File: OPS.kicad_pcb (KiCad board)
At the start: 4 copper layers, 49 x 34 mm, 92 parts, among them J1 USB, J2 PWR, J3 Banana, J4 Banana, J5 CON_PWR, J6 CON_DATA, J7 M3, P1 TC2030, Q1 SS8050, Q2 AO3400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

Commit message: started layout
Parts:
- moved C7 0.15 mm to (65.5, 64.8)
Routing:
- net SWDIO: track 0.00 -> 10.8 mm, vias 0 -> 1
- net SWCLK: track 0.00 -> 5.74 mm, vias 0 -> 1
- net Net-(J2-PadA5): track 0.00 -> 5.71 mm
- net Net-(C29-Pad2): track 0.00 -> 5.59 mm
- net Net-(J2-PadB5): track 0.00 -> 4.66 mm
- net UOUT: track 0.00 -> 3.66 mm
- net Net-(C29-Pad1): track 0.00 -> 3.59 mm
- net INT_MP_1: track 0.00 -> 3.58 mm
- net INT_MP: track 0.00 -> 3.35 mm
- net /UIN: track 0.00 -> 3.28 mm
- net Net-(D3-Pad2): track 0.00 -> 2.49 mm
- net TSENS: track 0.00 -> 2.43 mm
- net OUT: track 0.00 -> 2.32 mm
- net TREF: track 0.00 -> 2.29 mm
- net VBUS: track 0.00 -> 2.24 mm
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- added copper zone on F.Cu, net Net-(C13-Pad2)
- added copper zone on F.Cu, net Net-(C14-Pad2)
- added copper zone on F.Cu, net Net-(C15-Pad1)
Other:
- board text added: "OPS"

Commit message: routing 60%
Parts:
- C10, C15: value 100n -> 22u; footprint otter:C_0402 -> otter:C_0805
- C16, C20, C9: value 10u -> 22u
- C17, C8: footprint Capacitor_Tantalum_SMD:CP_EIA-7343-31_Kemet-D -> Capacitor_SMD:CP_Elec_6.3x5.8
- J6: footprint Connector_PinHeader_2.00mm:PinHeader_1x07_P2.00mm_Vertical -> Connector_PinHeader_2.00mm:PinHeader_1x08_P2.00mm_Vertical
- moved SW1 21.2 mm to (81.1, 52.1)
- moved J6 3.25 mm to (60.0, 52.4)
- moved J5 2.10 mm to (52.6, 74.2)
- moved C8 1.35 mm to (57.3, 77.2)
- moved C11 1.35 mm to (63.2, 82.5)
- moved R16 1.33 mm to (80.9, 67.7), turned to 0 degrees
- moved C17 1.25 mm to (74.5, 77.7)
- moved C9 0.66 mm to (61.6, 79.8)
- moved C15 0.54 mm to (68.7, 79.8)
- moved R10 0.53 mm to (63.2, 81.7)
- moved R14 0.50 mm to (63.2, 83.3)
- moved C26 0.50 mm to (70.0, 67.4)
- moved C32 0.50 mm to (69.1, 67.4)
- moved C33 0.50 mm to (68.2, 67.4)
- moved P1 0.46 mm to (76.8, 54.1), turned to 90 degrees
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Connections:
- J6 pad 4: OUT_EN_1 -> +3V3
- J6 pad 5: INT_MP_1 -> OUT_EN_1
- J6 pad 6: SCL -> INT_MP_1
- J6 pad 7: SDA -> SCL
- U3 pad 39: LED_RED -> LED_GREEN
- U3 pad 40: LED_GREEN -> LED_RED
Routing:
- net +3V3: track 1.01 -> 109.1 mm, vias 0 -> 7
- net GND: track 0.85 -> 54.6 mm, vias 1 -> 9
- net SDA: track 1.86 -> 46.0 mm, vias 0 -> 4
- net SCL: track 1.92 -> 42.4 mm, vias 0 -> 4
- net LED_RED: track 0.00 -> 39.5 mm, vias 0 -> 2
- net INT_MP: track 3.35 -> 35.4 mm, vias 0 -> 2
- net LED_GREEN: track 0.00 -> 30.5 mm, vias 0 -> 2
- net LED_ACT: track 0.00 -> 23.2 mm, vias 0 -> 2
- net VBUS: track 2.24 -> 23.2 mm, vias 0 -> 4
- net IOUT: track 2.00 -> 20.8 mm, vias 0 -> 2
- net IOUT_1: track 1.74 -> 19.1 mm, vias 0 -> 1
- net UOUT_2: track 1.64 -> 17.9 mm, vias 0 -> 1
- net TSENS_2: track 1.78 -> 17.1 mm, vias 0 -> 1
- net INT_STUSB: track 0.99 -> 15.2 mm, vias 0 -> 2
- net OUT_EN: track 0.00 -> 12.7 mm, vias 0 -> 2
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- added copper zone on B.Cu, net GND
- added copper zone on F.Cu, net GND
- added copper zone on F.Cu, net Net-(Q2-Pad2)
- added copper zone on F.Cu, net OUT
- added copper zone on F.Cu, net VBUS

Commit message: routing 99%
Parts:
- moved C8 2.00 mm to (57.3, 79.2)
- moved J5 2.00 mm to (52.6, 76.2)
- moved J2 1.85 mm to (57.0, 68.8)
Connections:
- SW1 pad 1: Net-(R5-Pad1) -> +3V3
- SW1 pad 2: +3V3 -> Net-(R5-Pad1)
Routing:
- net GND: track 54.6 -> 102.0 mm, vias 9 -> 101
- net UOUT: track 3.66 -> 36.9 mm, vias 0 -> 2
- net TSENS: track 2.31 -> 27.9 mm, vias 0 -> 2
- net VBUS: track 23.2 -> 41.9 mm
- net Net-(R5-Pad1): track 5.49 -> 20.0 mm, vias 0 -> 1
- net OUT_EN_1: track 2.02 -> 15.8 mm, vias 0 -> 3
- net INT_MP_1: track 3.58 -> 17.3 mm, vias 0 -> 3
- net Net-(Q1-Pad3): track 0.00 -> 9.08 mm
- net LED_GREEN: track 30.5 -> 38.1 mm
- net +3V3: track 109.1 -> 107.1 mm
- net D-: track 42.5 -> 44.3 mm
- net D+: track 41.3 -> 43.1 mm
- net Net-(J2-PadA5): track 5.71 -> 4.57 mm
- net IOUT_1: track 19.1 -> 20.2 mm
- net OUT_EN: track 12.7 -> 13.5 mm, vias 2 -> 4
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
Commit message: silk
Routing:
- net +3V3: track 107.1 -> 109.4 mm
- net SDA: track 46.6 -> 47.7 mm
- net INT_MP: track 35.4 -> 36.5 mm
- net SCL: track 42.8 -> 43.4 mm
- net UOUT: track 36.9 -> 37.5 mm
- net GND: track 102.0 -> 101.8 mm, vias 101 -> 103
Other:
- copper layers 4 -> 2
- board text added: "- +"
- board text added: "3V3"
- board text added: "DFU"
- board text added: "EN"
- board text added: "GND"
- board text added: "INT"
- board text added: "Iout"
- board text added: "MCU"
- board text added: "SCL"
- board text added: "SDA"
- board text added: "The Otter Power Supply Jan Henrik Hemsing 2021"
- board text added: "Tsns"
- board text added: "Uout"
- board text added: "Vin"
- board text added: "Vout 0-20.5V Iout 0-3A + typeK-In -"

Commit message: updated silk
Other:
- board text added: "Data"
- board text added: "Power"
- board text added: "The Otter Power Supply github.com/Jana-Marie/OPS @_Jana_Marie 2021"
- board text removed: "The Otter Power Supply Jan Henrik Hemsing 2021"
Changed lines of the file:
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@@
   (general
     (thickness 1.6)
-    (drawings 111)
+    (drawings 113)
     (tracks 966)
     (zones 0)
@@
   )
   (setup
-    (last_trace_width 0.15)
+    (last_trace_width 0.2)
     (user_trace_width 0.15)
     (user_trace_width 0.2)
@@
     (pcbplotparams
       (layerselection 0x010fc_ffffffff)
-      (usegerberextensions false)
+      (usegerberextensions true)
       (usegerberattributes false)
       (usegerberadvancedattributes false)
@@
       (psa4output false)
       (plotreference true)
-      (plotvalue true)
+      (plotvalue false)
       (plotinvisibletext false)
       (padsonsilk false)
@@
       (outputformat 1)
       (mirror false)
-      (drillshape 1)
+      (drillshape 0)
       (scaleselection 1)
-      (outputdirectory ""))
+      (outputdirectory "gerber/"))
   )
   (net 0 "")
@@
     )
   )
+  (gr_text Data (at 53.9 55.9 270) (layer B.SilkS)
+    (effects (font (size 1 1) (thickness 0.15)) (justify mirror))
+  )
+  (gr_text Power (at 53.9 68.75 270) (layer B.SilkS)
+    (effects (font (size 1 1) (thickness 0.15)) (justify mirror))
+  )
   (gr_line (start 93.35 77) (end 91.9 77) (layer B.SilkS) (width 0.12))
   (gr_line (start 93.35 72.85) (end 93.35 77) (layer B.SilkS) (width 0.12))
@@
     (effects (font (size 2 2) (thickness 0.15)) (justify mirror))
   )
-  (gr_text "The Otter Power Supply\nJan Henrik Hemsing\n2021" (at 58.3 65.95 180) (layer B.SilkS)
+  (gr_text "The Otter Power Supply\ngithub.com/Jana-Marie/OPS\n@_Jana_Marie  2021" (at 58.3 65.95 180) (layer B.SilkS)
     (effects (font (size 1 1) (thickness 0.15)) (justify left mirror))
   )
@@
   (segment (start 72.75 65.95) (end 72.152001 66.547999) (width 0.15) (layer F.Cu) (net 5))
   (segment (start 72.75 64.9125) (end 72.75 65.95) (width 0.15) (layer F.Cu) (net 5))
-  (segment (start 80.52 51.825) (end 80.125 51.43) (width 0.15) (layer B.Cu) (net 39))
-  (segment (start 80.125 51.43) (end 79.275 51.43) (width 0.15) (layer B.Cu) (net 39))
-  (segment (start 81.63 51.825) (end 80.52 51.825) (width 0.15) (layer B.Cu) (net 39))
-  (segment (start 82.025 51.43) (end 81.63 51.825) (width 0.15) (layer B.Cu) (net 39))
-  (segment (start 82.875 51.43) (end 82.025 51.43) (width 0.15) (layer B.Cu) (net 39))
   (segment (start 97.464999 68.874999) (end 97.174264 68.875) (width 0.15) (layer F.Cu) (net 5))
   (segment (start 97.49 68.9) (end 97.464999 68.874999) (width 0.15) (layer F.Cu) (net 5))
@@
   (segment (start 60.33 69.9) (end 59.65 70.58) (width 0.15) (layer F.Cu) (net 38))
   (segment (start 60.3375 69.9) (end 60.33 69.9) (width 0.15) (layer F.Cu) (net 38))
+  (segment (start 80.52 51.825) (end 80.125 51.43) (width 0.15) (layer B.Cu) (net 39))
+  (segment (start 80.125 51.43) (end 79.275 51.43) (width 0.15) (layer B.Cu) (net 39))
+  (segment (start 81.63 51.825) (end 80.52 51.825) (width 0.15) (layer B.Cu) (net 39))
+  (segment (start 82.025 51.43) (end 81.63 51.825) (width 0.15) (layer B.Cu) (net 39))
+  (segment (start 82.875 51.43) (end 82.025 51.43) (width 0.15) (layer B.Cu) (net 39))
   (segment (start 69.25 55.62) (end 69.25 56.5875) (width 0.15) (layer F.Cu) (net 39))
   (segment (start 69.67 55.2) (end 69.25 55.62) (width 0.15) (layer F.Cu) (net 39))

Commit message: updated to kicad 6
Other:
- net class Default removed

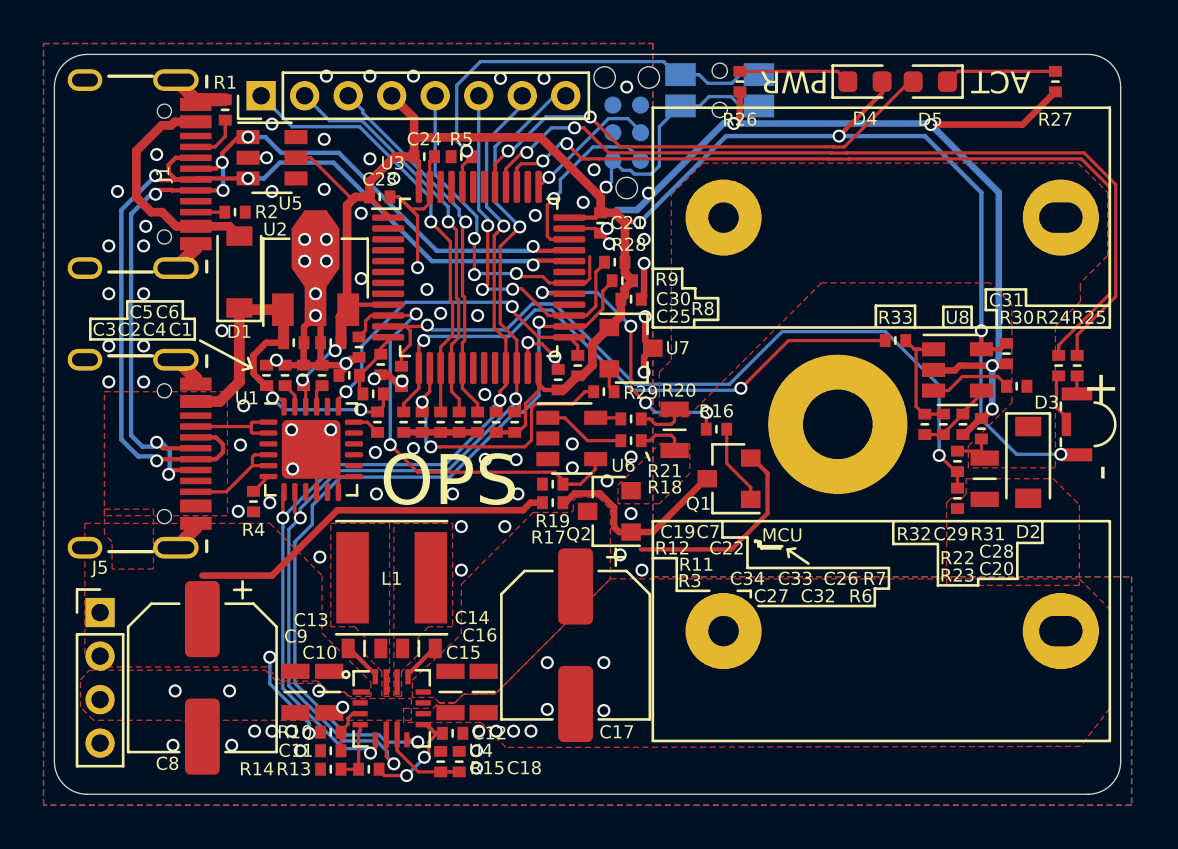
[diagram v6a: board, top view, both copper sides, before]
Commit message: updated layout, exchanged PMIC caps and inductor
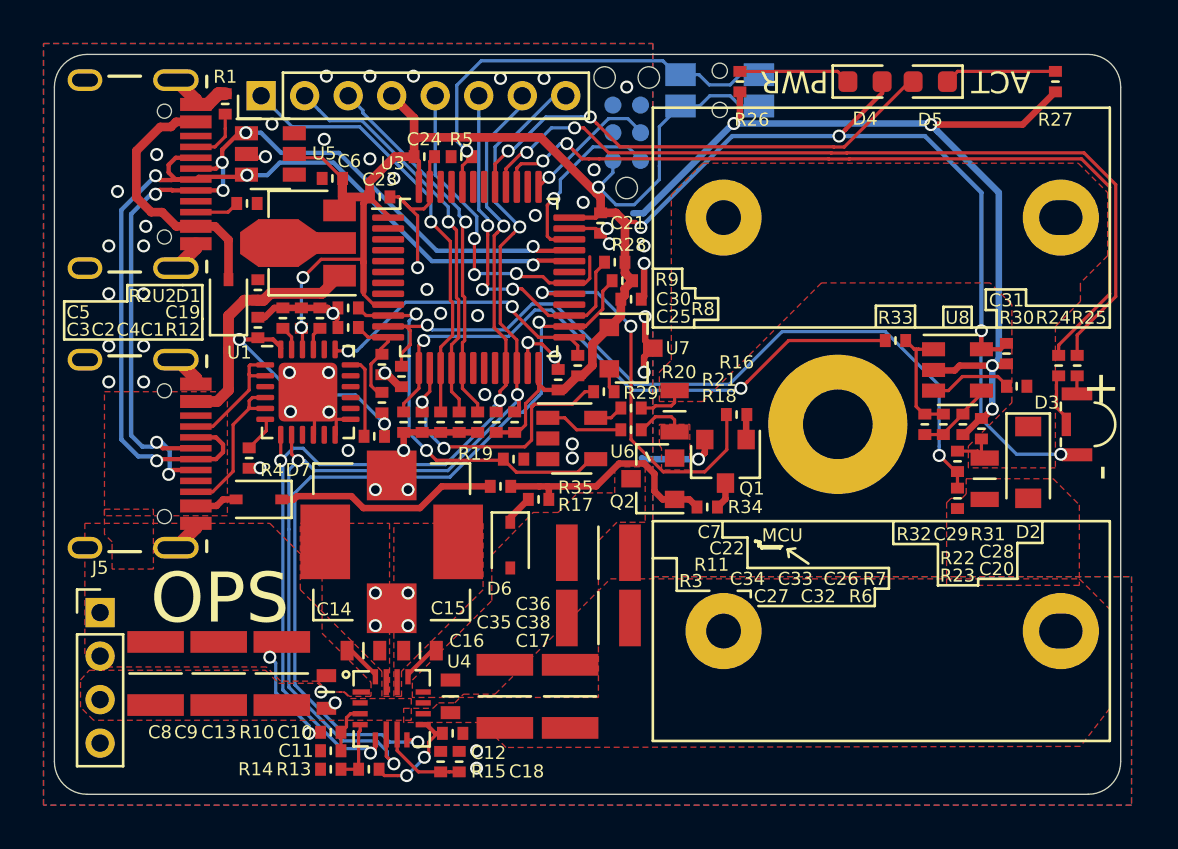
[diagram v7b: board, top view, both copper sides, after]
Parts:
- added C35: 22u, otter:C_1210, F.Cu at (71.2, 80.0)
- added C36: 22u, otter:C_1210, F.Cu at (75.5, 73.4)
- added C38: 22u, otter:C_1210, F.Cu at (75.5, 76.4)
- added D6: D_Small, Diode_SMD:D_SOD-323, F.Cu at (71.5, 73.0)
- added D7: D_Small, Diode_SMD:D_SOD-323, F.Cu at (59.9, 71.0)
- added R34: 2k37, otter:R_0402, F.Cu at (80.5, 71.3)
- added R35: 5k1, otter:R_0402, F.Cu at (71.0, 70.3)
- C10, C15, C16: value 22u -> 100n; footprint otter:C_0805 -> otter:C_0603
- C13: value 100n -> 22u; footprint otter:C_0603 -> otter:C_1210
- C17, C8: value 47u -> 22u; footprint Capacitor_SMD:CP_Elec_6.3x5.8 -> otter:C_1210
- C9: footprint otter:C_0805 -> otter:C_1210
- D1: value SS34 -> D_Small; footprint Diode_SMD:D_SOD-123 -> Diode_SMD:D_SOD-323
- L1: value 4u7 -> IHLE-2525CD; footprint Inductor_SMD:L_Taiyo-Yuden_MD-5050 -> otter:IHLE-2525CD
- moved C6 7.55 mm to (63.3, 56.2)
- moved C13 3.97 mm to (61.0, 79.0), turned to -90 degrees
- moved C9 3.63 mm to (58.0, 79.0)
- moved C5 2.93 mm to (59.9, 61.3), turned to 90 degrees
- moved U1 2.64 mm to (62.1, 66.0)
- moved C2 2.63 mm to (61.0, 62.6)
- moved C4 2.63 mm to (61.9, 62.6)
- moved C1 2.63 mm to (62.7, 62.6)
- moved C14 2.55 mm to (64.7, 77.9), turned to 0 degrees
- moved Q2 2.50 mm to (78.0, 70.0)
- moved C17 2.36 mm to (74.2, 80.0)
- moved C15 2.36 mm to (67.3, 77.9), turned to 180 degrees
- moved C3 2.24 mm to (59.9, 63.0)
- moved R12 2.20 mm to (64.0, 63.0)
- moved C8 2.16 mm to (55.1, 79.0)
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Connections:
- C13 pad 1: Net-(C13-Pad1) -> VBUS
- C13 pad 2: Net-(C13-Pad2) -> GND
- C15 pad 2: GND -> Net-(C15-Pad2)
- C16 pad 1: Net-(C15-Pad1) -> Net-(C16-Pad1)
- C17 pad 1: Net-(C15-Pad1) -> Net-(C16-Pad1)
- J1 pad A8: Net-(J1-PadA8) -> unconnected-(J1-PadA8)
- J1 pad B8: Net-(J1-PadB8) -> unconnected-(J1-PadB8)
- J2 pad A8: Net-(J2-PadA8) -> unconnected-(J2-PadA8)
- J2 pad B8: Net-(J2-PadB8) -> unconnected-(J2-PadB8)
- J7 pad 1: Net-(J7-Pad1) -> unconnected-(J7-Pad1)
- L1 pad 1: Net-(C13-Pad2) -> Net-(C14-Pad2)
- L1 pad 2: Net-(C14-Pad2) -> Net-(C15-Pad2)
- P1 pad 3: Net-(P1-Pad3) -> unconnected-(P1-Pad3)
- P1 pad 6: Net-(P1-Pad6) -> unconnected-(P1-Pad6)
- Q2 pad 1: Net-(Q1-Pad3) -> Net-(Q2-Pad1)
- Q2 pad 3: Net-(C15-Pad1) -> Net-(C16-Pad1)
- R17 pad 1: VBUS -> Net-(D6-Pad1)
- R17 pad 2: Net-(Q1-Pad3) -> Net-(Q2-Pad1)
- U1 pad 11: Net-(U1-Pad11) -> unconnected-(U1-Pad11)
- U1 pad 14: Net-(U1-Pad14) -> unconnected-(U1-Pad14)
- U1 pad 15: Net-(U1-Pad15) -> unconnected-(U1-Pad15)
- U1 pad 16: Net-(U1-Pad16) -> unconnected-(U1-Pad16)
- U1 pad 17: Net-(U1-Pad17) -> unconnected-(U1-Pad17)
- U1 pad 20: Net-(U1-Pad20) -> unconnected-(U1-Pad20)
- U1 pad 3: Net-(U1-Pad3) -> unconnected-(U1-Pad3)
- U1 pad 9: Net-(U1-Pad9) -> unconnected-(U1-Pad9)
- U3 pad 18: Net-(U3-Pad18) -> unconnected-(U3-Pad18)
- U3 pad 19: Net-(U3-Pad19) -> unconnected-(U3-Pad19)
- U3 pad 2: Net-(U3-Pad2) -> unconnected-(U3-Pad2)
- U3 pad 20: Net-(U3-Pad20) -> unconnected-(U3-Pad20)
- U3 pad 28: Net-(U3-Pad28) -> unconnected-(U3-Pad28)
- U3 pad 3: Net-(U3-Pad3) -> unconnected-(U3-Pad3)
- U3 pad 31: Net-(U3-Pad31) -> unconnected-(U3-Pad31)
- U3 pad 38: Net-(U3-Pad38) -> unconnected-(U3-Pad38)
- U3 pad 4: Net-(U3-Pad4) -> unconnected-(U3-Pad4)
- U3 pad 42: Net-(U3-Pad42) -> unconnected-(U3-Pad42)
- U3 pad 43: Net-(U3-Pad43) -> unconnected-(U3-Pad43)
- U3 pad 45: Net-(U3-Pad45) -> unconnected-(U3-Pad45)
- U3 pad 46: Net-(U3-Pad46) -> unconnected-(U3-Pad46)
- U3 pad 5: Net-(U3-Pad5) -> unconnected-(U3-Pad5)
- U3 pad 6: Net-(U3-Pad6) -> unconnected-(U3-Pad6)
- U3 pad 7: Net-(U3-Pad7) -> unconnected-(U3-Pad7)
- U4 pad 12: Net-(C15-Pad1) -> Net-(C16-Pad1)
- U4 pad 13: Net-(C14-Pad1) -> Net-(C15-Pad1)
- U4 pad 14: Net-(C14-Pad2) -> Net-(C15-Pad2)
- U4 pad 15: Net-(C13-Pad2) -> Net-(C14-Pad2)
- U4 pad 16: Net-(C13-Pad1) -> Net-(C14-Pad1)
- U5 pad 4: Net-(U5-Pad4) -> unconnected-(U5-Pad4)
- U5 pad 6: Net-(U5-Pad6) -> unconnected-(U5-Pad6)
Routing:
- net VBUS: track 41.9 -> 30.4 mm
- net GND: track 101.8 -> 90.6 mm, vias 103 -> 64
- net Net-(Q2-Pad1): track 0.00 -> 11.1 mm
- net Net-(D7-Pad1): track 0.00 -> 10.3 mm
- net Net-(Q1-Pad3): track 9.08 -> 1.25 mm
- net OUT_EN: track 13.5 -> 18.2 mm, vias 4 -> 2
- net +3V3: track 109.4 -> 112.6 mm
- net IOUT: track 20.8 -> 18.0 mm
- net Net-(Q1-Pad1): track 3.68 -> 1.16 mm
- net Net-(R3-Pad1): track 1.28 -> 3.79 mm
- net SCL: track 43.4 -> 45.7 mm
- net Net-(J2-PadB5): track 5.01 -> 7.21 mm
- net SDA: track 47.7 -> 49.7 mm
- net INT_STUSB: track 15.4 -> 13.4 mm
- net Net-(C15-Pad1): track 0.00 -> 1.85 mm
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- added copper zone on F.Cu, net Net-(C15-Pad2)
- added copper zone on F.Cu, net Net-(C16-Pad1)
- removed copper zone on F.Cu, net Net-(C13-Pad2)
- removed copper zone on F.Cu, net Net-(C15-Pad1)
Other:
- board text added: "The Otter Power Supply github.com/Jana-Marie/OPS @_Jana_Marie 2022 v1.1"
- board text removed: "The Otter Power Supply github.com/Jana-Marie/OPS @_Jana_Marie 2021"

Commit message: update
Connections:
- U4 pad 11: (no net) -> GND
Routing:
- net GND: track 90.6 -> 92.0 mm
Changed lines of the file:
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@@
   (net 92 "Net-(D6-Pad1)")
   (net 93 "Net-(D7-Pad1)")
-  (net 94 "Net-(J1-PadA4)")
+  (net 94 "Net-(D1-Pad2)")
   (footprint "otter:C_0402" (layer "F.Cu")
     (at 62.7 62.61875 90)
@@
       (net 4 "VBUS") (pinfunction "K") (pintype "passive"))
     (pad "2" smd rect (at 1.05 0 90) (size 0.6 0.45) (layers "F.Cu" "F.Paste" "F.Mask")
-      (net 94 "Net-(J1-PadA4)") (pinfunction "A") (pintype "passive"))
+      (net 94 "Net-(D1-Pad2)") (pinfunction "A") (pintype "passive"))
     (model "${KICAD6_3DMODEL_DIR}/Diode_SMD.3dshapes/D_SOD-323.wrl"
       (offset (xyz 0 0 0))
@@
       (net 1 "GND") (pinfunction "GND") (pintype "power_in"))
     (pad "A4" smd rect (at -2.4 0 270) (size 0.6 1.45) (layers "F.Cu" "F.Paste" "F.Mask")
-      (net 94 "Net-(J1-PadA4)") (pinfunction "VBUS") (pintype "power_in"))
+      (net 94 "Net-(D1-Pad2)") (pinfunction "VBUS") (pintype "power_in"))
     (pad "A5" smd rect (at -1.25 0 270) (size 0.3 1.45) (layers "F.Cu" "F.Paste" "F.Mask")
       (net 18 "Net-(J1-PadA5)") (pinfunction "CC1") (pintype "bidirectional"))
@@
       (net 43 "unconnected-(J1-PadA8)") (pinfunction "SBU1") (pintype "bidirectional+no_connect"))
     (pad "A9" smd rect (at -2.4 0 270) (size 0.6 1.45) (layers "F.Cu" "F.Paste" "F.Mask")
-      (net 94 "Net-(J1-PadA4)") (pinfunction "VBUS") (pintype "passive"))
+      (net 94 "Net-(D1-Pad2)") (pinfunction "VBUS") (pintype "passive"))
     (pad "A12" smd rect (at -3.2 0 270) (size 0.6 1.45) (layers "F.Cu" "F.Paste" "F.Mask")
       (net 1 "GND") (pinfunction "GND") (pintype "passive"))
@@
       (net 1 "GND") (pinfunction "GND") (pintype "passive"))
     (pad "B4" smd rect (at 2.4 0 270) (size 0.6 1.45) (layers "F.Cu" "F.Paste" "F.Mask")
-      (net 94 "Net-(J1-PadA4)") (pinfunction "VBUS") (pintype "passive"))
+      (net 94 "Net-(D1-Pad2)") (pinfunction "VBUS") (pintype "passive"))
     (pad "B5" smd rect (at 1.75 0 270) (size 0.3 1.45) (layers "F.Cu" "F.Paste" "F.Mask")
       (net 14 "Net-(J1-PadB5)") (pinfunction "CC2") (pintype "bidirectional"))
@@
       (net 44 "unconnected-(J1-PadB8)") (pinfunction "SBU2") (pintype "bidirectional+no_connect"))
     (pad "B9" smd rect (at 2.4 0 270) (size 0.6 1.45) (layers "F.Cu" "F.Paste" "F.Mask")
-      (net 94 "Net-(J1-PadA4)") (pinfunction "VBUS") (pintype "passive"))
+      (net 94 "Net-(D1-Pad2)") (pinfunction "VBUS") (pintype "passive"))
     (pad "B12" smd rect (at 3.2 0 270) (size 0.6 1.45) (layers "F.Cu" "F.Paste" "F.Mask")
       (net 1 "GND") (pinfunction "GND") (pintype "passive"))
@@
     (pad "10" smd rect locked (at 1.45 0.25 180) (size 0.7 0.25) (layers "F.Cu" "F.Paste" "F.Mask")
       (net 1 "GND") (pinfunction "AGND") (pintype "input"))
-    (pad "11" smd rect locked (at 1.45 -0.25 180) (size 0.7 0.25) (layers "F.Cu" "F.Paste" "F.Mask"))
+    (pad "11" smd rect locked (at 1.45 -0.25 180) (size 0.7 0.25) (layers "F.Cu" "F.Paste" "F.Mask")
+      (net 1 "GND") (pinfunction "GND") (pintype "input"))
     (pad "12" smd rect locked (at 1.45 -0.75 180) (size 0.7 0.25) (layers "F.Cu" "F.Paste" "F.Mask")
       (net 24 "Net-(C16-Pad1)") (pinfunction "OUT") (pintype "input"))
@@
   (segment (start 82 53.4) (end 81.725 53.675) (width 0.3) (layer "F.Cu") (net 1))
   (segment (start 73.65 64.55) (end 73.5 64.4) (width 0.15) (layer "F.Cu") (net 1))
+  (segment (start 68.25 80.3) (end 68.7 80.75) (width 0.2) (layer "F.Cu") (net 1))
   (segment (start 66.320195 65.77) (end 66.45 65.77) (width 0.3) (layer "F.Cu") (net 1))
   (segment (start 65.42 65.22) (end 65.5 65.22) (width 0.15) (layer "F.Cu") (net 1))
@@
   (segment (start 67.475 57.6) (end 66.87 57.6) (width 0.15) (layer "F.Cu") (net 1))
   (segment (start 57 72.05) (end 57 72.255) (width 0.6) (layer "F.Cu") (net 1))
+  (segment (start 67.45 80.3) (end 68.25 80.3) (width 0.2) (layer "F.Cu") (net 1))
   (segment (start 69.95 67.87) (end 66.55 67.87) (width 0.3) (layer "F.Cu") (net 1))
   (segment (start 57 65.395) (end 56.085 64.48) (width 0.6) (layer "F.Cu") (net 1))
